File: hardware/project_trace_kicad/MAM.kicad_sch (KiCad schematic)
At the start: 1 part, among them U503 NUCLEO-H753ZI

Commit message: Add missing Part-numers, Revise AC Coupling
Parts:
- U503: DigikeyPN (none) -> N/A
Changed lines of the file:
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@@
+			)
+		)
+		(property "DigikeyPN" "N/A"
+			(at 77.47 49.53 0)
+			(hide yes)
+			(show_name no)
+			(do_not_autoplace no)
+			(effects
+				(font
+					(size 1.27 1.27)
+				)
 			)
 		)
@@
 			)
 		)
+		(property "DigikeyPN" "N/A"
+			(at 179.07 128.27 0)
+			(hide yes)
+			(show_name no)
+			(do_not_autoplace no)
+			(effects
+				(font
+					(size 1.27 1.27)
+				)
+			)
+		)
 		(pin "9_12"
 		)
@@
 			)
 		)
+		(property "DigikeyPN" "N/A"
+			(at 147.32 52.07 0)
+			(hide yes)
+			(show_name no)
+			(do_not_autoplace no)
+			(effects
+				(font
+					(size 1.27 1.27)
+				)
+			)
+		)
 		(pin "9_12"
 		)
@@
 			)
 		)
+		(property "DigikeyPN" "N/A"
+			(at 80.01 127 0)
+			(hide yes)
+			(show_name no)
+			(do_not_autoplace no)
+			(effects
+				(font
+					(size 1.27 1.27)
+				)
+			)
+		)
 		(pin "9_12"
 		)
@@
 			(hide yes)
 			(show_name no)
+			(do_not_autoplace no)
+			(effects
+				(font
+					(size 1.27 1.27)
+				)
+			)
+		)
+		(property "DigikeyPN" "N/A"
+			(at 213.36 55.88 0)
+			(hide yes)
+			(show_name no)

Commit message: UI updated, CLK implemented, Parts labeled as Donotplace in power
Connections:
- net 40MHz.clk.out: no longer names the net of U503.8_4 (PC9)
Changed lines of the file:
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@@
 	(wire
 		(pts
-			(xy 227.33 49.53) (xy 231.14 49.53)
+			(xy 130.81 50.8) (xy 133.35 50.8)
+		)
+		(stroke
+			(width 0)
+			(type default)
+		)
+	)
+	(wire
+		(pts
+			(xy 130.81 58.42) (xy 133.35 58.42)
 		)
 		(stroke
@@
 		)
 	)
-	(hierarchical_label "40MHz.clk.out"
-		(shape output)
-		(at 231.14 49.53 0)
-		(effects
-			(font
-				(size 1.27 1.27)
-			)
-			(justify left)
-		)
-	)
+	(hierarchical_label "V.meter"
+		(shape output)
+		(at 130.81 43.18 180)
+		(effects
+			(font
+				(size 1.27 1.27)
+			)
+			(justify right)
+		)
+	)

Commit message: Hierarchical pins for clk added, CLK resistance in MAM added
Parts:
- added R501: 100, ProjectTraceFootprints:RN73R2ATTD1000B25, symbol Device:R
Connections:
- net CLK.EN: now reaches U503.8_2 (PC8)
- net at U503.8_4 (PC9): now also R501.1
- new net 40MHz.CLK.Out: R501.2
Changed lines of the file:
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@@
-	(wire
-		(pts
-			(xy 161.29 63.5) (xy 163.83 63.5)
-		)
-		(stroke
-			(width 0)
-			(type default)
-		)
-	)
 	(wire
 		(pts
@@
 	(wire
 		(pts
+			(xy 227.33 49.53) (xy 238.76 49.53)
+		)
+		(stroke
+			(width 0)
+			(type default)
+		)
+	)
+	(wire
+		(pts
 			(xy 194.31 138.43) (xy 198.12 138.43)
 		)
@@
 	(wire
 		(pts
+			(xy 246.38 49.53) (xy 247.65 49.53)
+		)
+		(stroke
+			(width 0)
+			(type default)
+		)
+	)
+	(wire
+		(pts
 			(xy 59.69 39.37) (xy 62.23 39.37)
 		)
@@
 	(wire
 		(pts
-			(xy 161.29 53.34) (xy 163.83 53.34)
-		)
-		(stroke
-			(width 0)
-			(type default)
-		)
-	)
-	(wire
-		(pts
 			(xy 59.69 39.37) (xy 59.69 41.91)
 		)
@@
 	(wire
 		(pts
-			(xy 227.33 52.07) (xy 231.14 52.07)
+			(xy 227.33 52.07) (xy 228.6 52.07)
 		)
 		(stroke
@@
 	(wire
 		(pts
-			(xy 194.31 128.27) (xy 198.12 128.27)
-		)
-		(stroke
-			(width 0)
-			(type default)
-		)
-	)
-	(wire
-		(pts
 			(xy 129.54 60.96) (xy 133.35 60.96)
 		)
@@
 	(wire
 		(pts
-			(xy 194.31 125.73) (xy 198.12 125.73)
+			(xy 227.33 46.99) (xy 228.6 46.99)
 		)
 		(stroke
@@
 		)
 	)
+	(hierarchical_label "CLK.EN"
+		(shape output)
+		(at 228.6 46.99 0)
+		(effects
+			(font
+				(size 1.27 1.27)
+			)
+			(justify left)
+		)
+	)
 	(hierarchical_label "SPI3.MOSI"
 		(shape output)
@@
 		)
 	)
+	(hierarchical_label "40MHz.CLK.Out"
+		(shape output)
+		(at 247.65 49.53 0)
+		(effects
+			(font
+				(size 1.27 1.27)
+			)
+			(justify left)
+		)
+	)
 	(hierarchical_label "SW3.B"
 		(shape input)
@@
 	(hierarchical_label "SPI3.SCK"
 		(shape output)
-		(at 231.14 52.07 0)
+		(at 228.6 52.07 0)
 		(effects
 			(font
@@
 				)
 			)
+		)
+	)
+	(symbol
+		(lib_id "Device:R")
+		(at 242.57 49.53 90)
+		(unit 1)
+		(body_style 1)
+		(exclude_from_sim no)
+		(in_bom yes)
+		(on_board yes)
+		(in_pos_files yes)
+		(dnp no)
+		(fields_autoplaced yes)
+		(property "Reference" "R501"
+			(at 242.57 44.3695 90)
+			(show_name no)
+			(do_not_autoplace no)
+			(effects
+				(font
+					(size 1.27 1.27)
+				)
+			)
+		)
+		(property "Value" "100"
+			(at 242.57 46.7938 90)
+			(show_name no)
+			(do_not_autoplace no)
+			(effects
+				(font
+					(size 1.27 1.27)
+				)
+			)
+		)
+		(property "Footprint" "ProjectTraceFootprints:RN73R2ATTD1000B25"
+			(at 242.57 51.308 90)
+			(hide yes)
+			(show_name no)
+			(do_not_autoplace no)
+			(effects
+				(font
+					(size 1.27 1.27)
+				)
+			)
+		)
+		(property "Datasheet" ""
+			(at 242.57 49.53 0)
+			(hide yes)
+			(show_name no)
+			(do_not_autoplace no)
+			(effects
+				(font
+					(size 1.27 1.27)
+				)
+			)
+		)
+		(property "Description" "Resistor"
+			(at 242.57 49.53 0)
+			(hide yes)
+			(show_name no)
+			(do_not_autoplace no)
+			(effects
+				(font
+					(size 1.27 1.27)
+				)
+			)
+		)
+		(property "DigikeyPN" "2019-RN73R2ATTD1000B25CT-ND"
+			(at 242.57 49.53 90)
+			(hide yes)
+			(show_name no)
+			(do_not_autoplace no)
+			(effects
+				(font
+					(size 1.27 1.27)
+				)
+			)
+		)
+		(pin "1"
+		)
+		(pin "2"
+		)
+		(instances
+			(project "project_trace_kicad"
+				(path "/af51f4e5-b952-4b0e-baf2-78a72fb86fcd/aebaf62e-54ce-46f5-a91f-d86d07c0b2fa"
+					(reference "R501")
+					(unit 1)
+				)
+			)

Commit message: PN removed from items not to be ordered and BOM generated/updated
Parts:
- U503: DigikeyPN N/A -> (none)
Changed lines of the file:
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@@
-			)
-		)
-		(property "DigikeyPN" "N/A"
-			(at 77.47 49.53 0)
-			(hide yes)
-			(show_name no)
-			(do_not_autoplace no)
-			(effects
-				(font
-					(size 1.27 1.27)
-				)
 			)
 		)
@@
 			)
 		)
-		(property "DigikeyPN" "N/A"
-			(at 179.07 128.27 0)
-			(hide yes)
-			(show_name no)
-			(do_not_autoplace no)
-			(effects
-				(font
-					(size 1.27 1.27)
-				)
-			)
-		)
 		(pin "9_12"
 		)
@@
 			)
 		)
-		(property "DigikeyPN" "N/A"
-			(at 147.32 52.07 0)
-			(hide yes)
-			(show_name no)
-			(do_not_autoplace no)
-			(effects
-				(font
-					(size 1.27 1.27)
-				)
-			)
-		)
 		(pin "9_12"
 		)
@@
 			)
 		)
-		(property "DigikeyPN" "N/A"
-			(at 80.01 127 0)
-			(hide yes)
-			(show_name no)
-			(do_not_autoplace no)
-			(effects
-				(font
-					(size 1.27 1.27)
-				)
-			)
-		)
 		(pin "9_12"
 		)
@@
 			(hide yes)
 			(show_name no)
-			(do_not_autoplace no)
-			(effects
-				(font
-					(size 1.27 1.27)
-				)
-			)
-		)
-		(property "DigikeyPN" "N/A"
-			(at 213.36 55.88 0)
-			(hide yes)
-			(show_name no)

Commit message: Further PCB development
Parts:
- U503: DigikeyPN (none) -> 2057-PH2-80-UA-ND AND 2057-PH2-20-UA-ND
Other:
- note added: "TODO fix digikeyPN for headers"
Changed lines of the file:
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@@
 		(company "Alexander N. Olsen")
+	)
+	(text "TODO fix digikeyPN for headers\n"
+		(exclude_from_sim no)
+		(at 129.032 95.25 0)
+		(effects
+			(font
+				(size 1.27 1.27)
+			)
+		)
 	)
 	(junction
@@
 			)
 		)
+		(property "DigikeyPN" "2057-PH2-80-UA-ND AND 2057-PH2-20-UA-ND"
+			(at 77.47 49.53 0)
+			(hide yes)
+			(show_name no)
+			(do_not_autoplace no)
+			(effects
+				(font
+					(size 1.27 1.27)
+				)
+			)
+		)
 		(pin "9_12"
 		)
@@
 			)
 		)
+		(property "DigikeyPN" "2057-PH2-80-UA-ND AND 2057-PH2-20-UA-ND"
+			(at 179.07 128.27 0)
+			(hide yes)
+			(show_name no)
+			(do_not_autoplace no)
+			(effects
+				(font
+					(size 1.27 1.27)
+				)
+			)
+		)
 		(pin "9_12"
 		)
@@
 			)
 		)
+		(property "DigikeyPN" "2057-PH2-80-UA-ND AND 2057-PH2-20-UA-ND"
+			(at 147.32 52.07 0)
+			(hide yes)
+			(show_name no)
+			(do_not_autoplace no)
+			(effects
+				(font
+					(size 1.27 1.27)
+				)
+			)
+		)
 		(pin "9_12"
 		)
@@
 			)
 		)
+		(property "DigikeyPN" "2057-PH2-80-UA-ND AND 2057-PH2-20-UA-ND"
+			(at 80.01 127 0)
+			(hide yes)
+			(show_name no)
+			(do_not_autoplace no)
+			(effects
+				(font
+					(size 1.27 1.27)
+				)
+			)
+		)
 		(pin "9_12"
 		)
@@
 			(hide yes)
 			(show_name no)
+			(do_not_autoplace no)
+			(effects
+				(font
+					(size 1.27 1.27)
+				)
+			)
+		)
+		(property "DigikeyPN" "2057-PH2-80-UA-ND AND 2057-PH2-20-UA-ND"
+			(at 213.36 55.88 0)
+			(hide yes)
+			(show_name no)

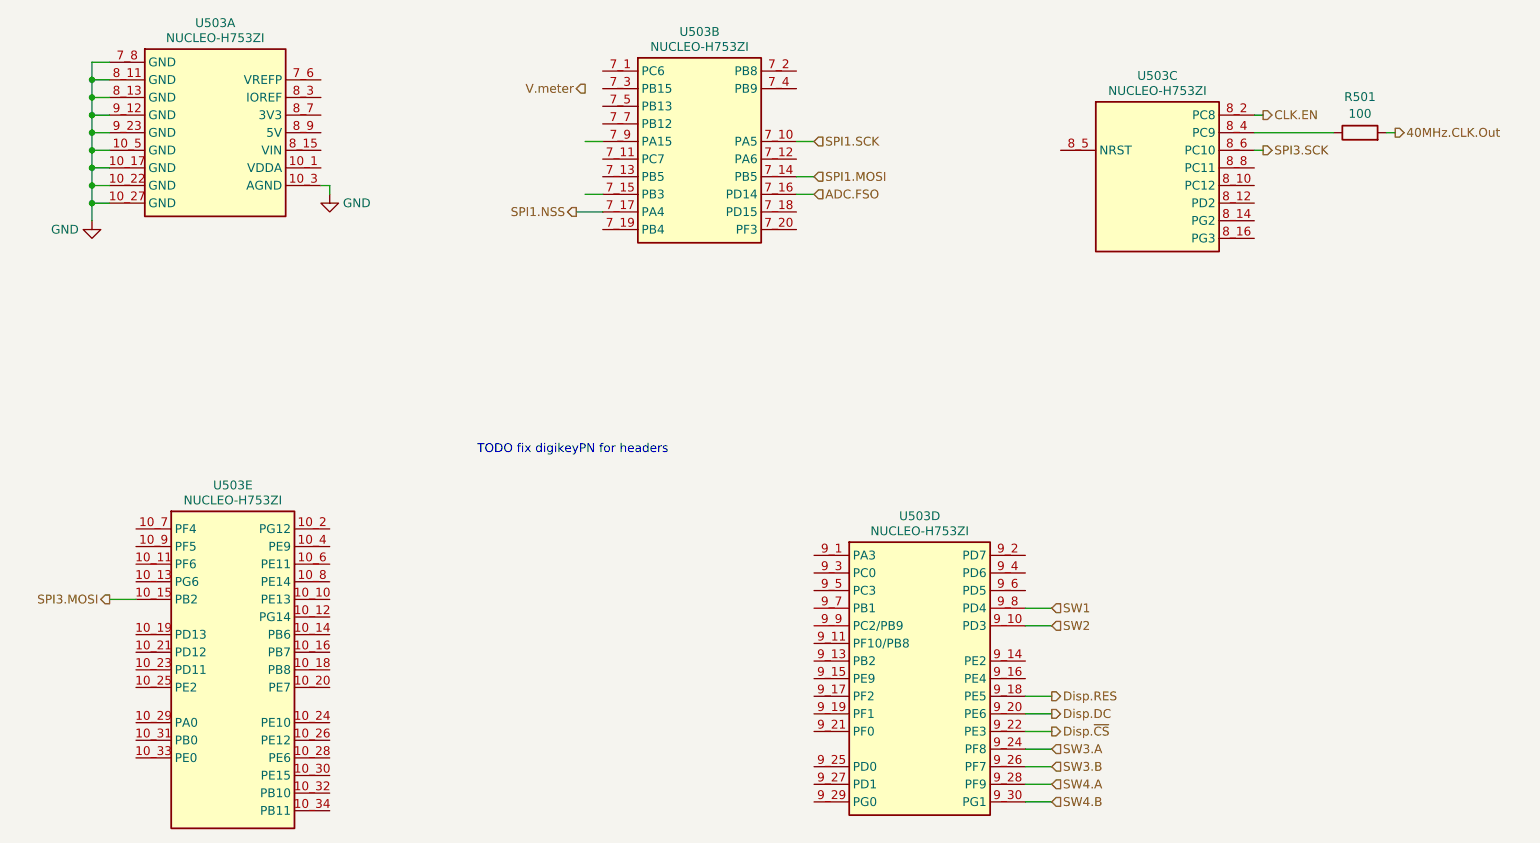
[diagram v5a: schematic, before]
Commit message: ERC Checks & Bug-Fixing
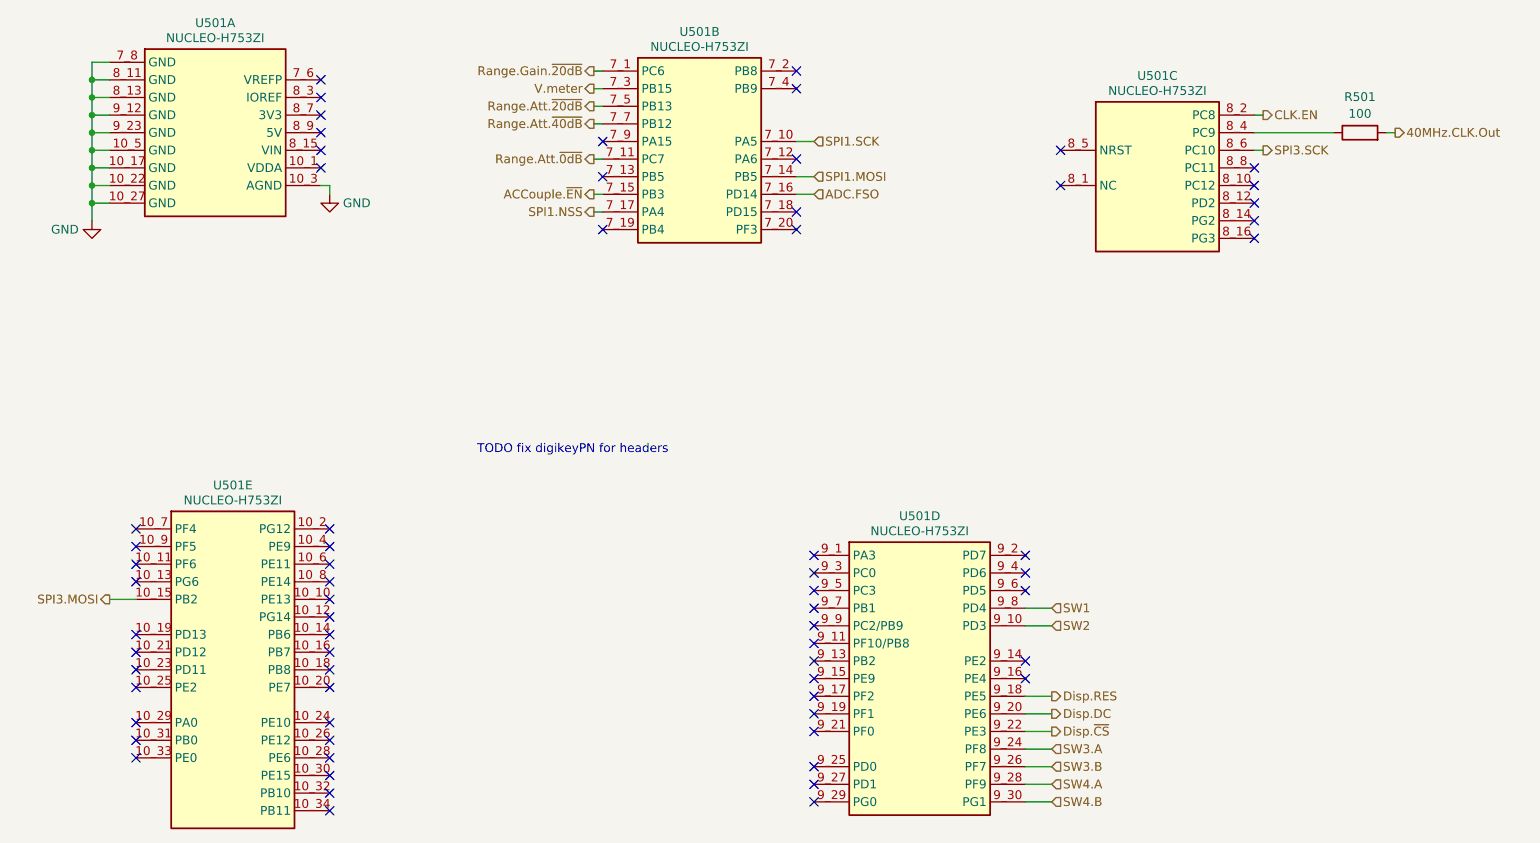
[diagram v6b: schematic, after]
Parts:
- renumbered U503 to U501
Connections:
- net V.meter: now also U501.7_3 (PB15)
- net Range.Gain.~{20dB}: now reaches U501.7_1 (PC6)
- net Range.Att.~{0dB}: now reaches U501.7_11 (PC7)
- net ACCouple.~{EN}: now reaches U501.7_15 (PB3)
- net Range.Att.~{20dB}: now reaches U501.7_5 (PB13)
- net Range.Att.~{40dB}: now reaches U501.7_7 (PB12)
- no-connect marks 0 -> 67
